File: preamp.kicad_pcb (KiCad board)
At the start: 2 copper layers, 70 x 67 mm, 69 parts, among them J1 AC, J2 JST_XH_3, J3 JST_XH_3, J4 JST_XH_3, J6 JST_XH_3, SW1 SW_SPST, SW2 SW_SPST, U1 L78L09_SOT89, U2 L78L05_SOT89, U3 NJM2753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

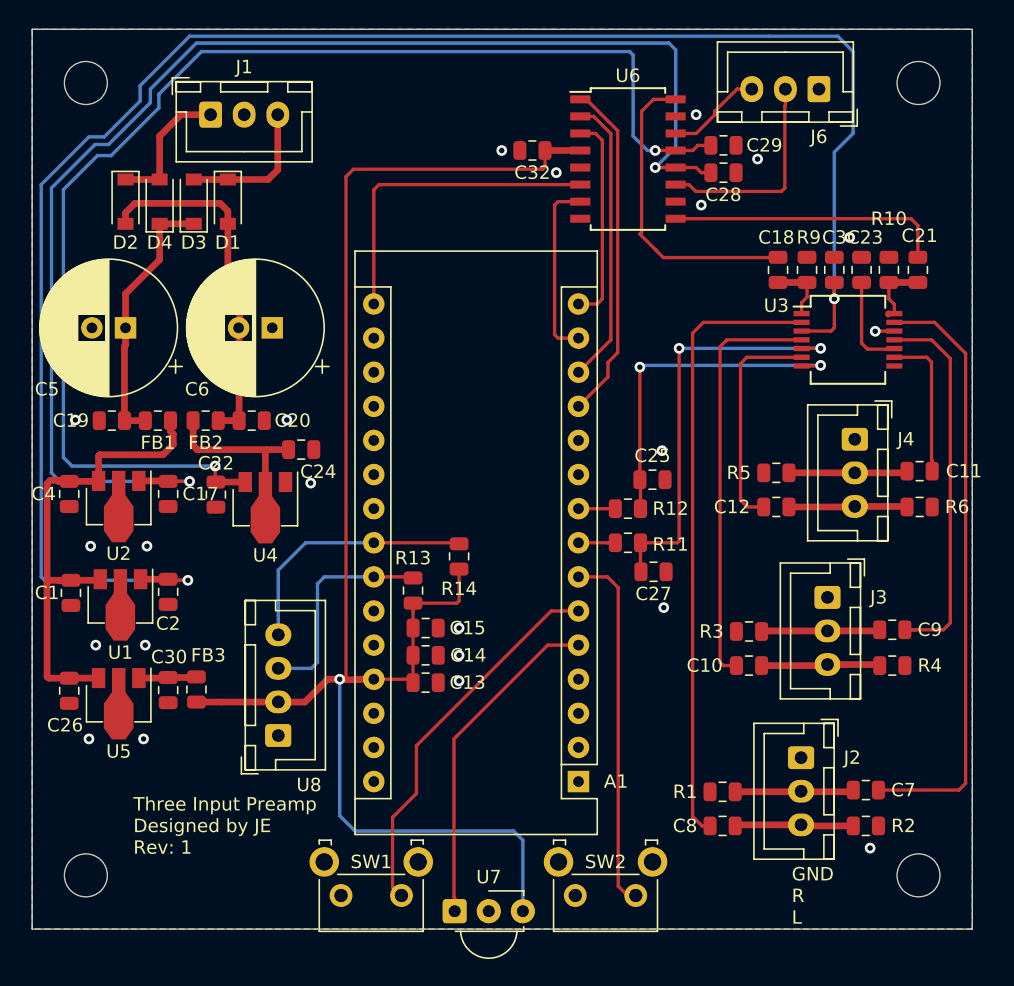
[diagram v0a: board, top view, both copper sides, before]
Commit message: updated silkscreen
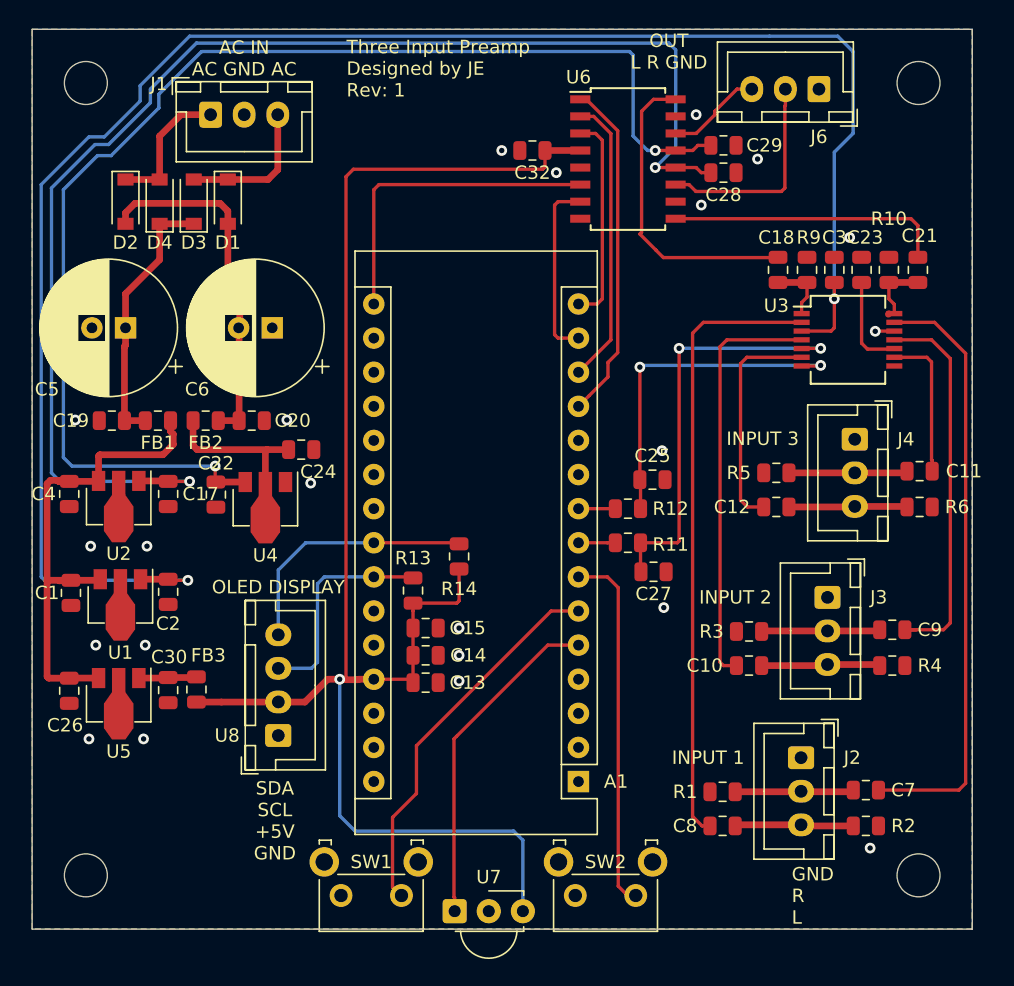
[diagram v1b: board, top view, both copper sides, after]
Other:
- board text added: "AC IN AC GND AC"
- board text added: "INPUT 1"
- board text added: "INPUT 2"
- board text added: "INPUT 3"
- board text added: "OLED DISPLAY"
- board text added: "OUT L R GND"
- board text added: "SDA SCL +5V GND"
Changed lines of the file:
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@@
-(kicad_pcb (version 20171130) (host pcbnew "(5.1.0)-1")
+(kicad_pcb (version 20171130) (host pcbnew 5.0.2-bee76a0~70~ubuntu18.04.1)
   (general
     (thickness 1.6)
-    (drawings 7)
+    (drawings 14)
     (tracks 353)
     (zones 0)
@@
     (zone_45_only no)
     (trace_min 0.2)
+    (segment_width 0.2)
+    (edge_width 0.05)
     (via_size 0.8)
     (via_drill 0.4)
@@
     (uvia_min_size 0.2)
     (uvia_min_drill 0.1)
-    (edge_width 0.05)
-    (segment_width 0.2)
     (pcb_text_width 0.3)
     (pcb_text_size 1.5 1.5)
@@
     (descr "JST XH series connector, B4B-XH-A (http://www.jst-mfg.com/product/pdf/eng/eXH.pdf), generated with kicad-footprint-generator")
     (tags "connector JST XH vertical")
-    (fp_text reference U8 (at -3.683 2.286 180) (layer F.SilkS)
+    (fp_text reference U8 (at 0 -3.81 180) (layer F.SilkS)
       (effects (font (size 1 1) (thickness 0.15)))
     )
@@
     (tags "SOIC 1.27")
     (attr smd)
-    (fp_text reference U6 (at 0 -6.2) (layer F.SilkS)
+    (fp_text reference U6 (at -3.683 -6.096) (layer F.SilkS)
       (effects (font (size 1 1) (thickness 0.15)))
     )
@@
     (descr "JST XH series connector, B3B-XH-A (http://www.jst-mfg.com/product/pdf/eng/eXH.pdf), generated with kicad-footprint-generator")
     (tags "connector JST XH vertical")
-    (fp_text reference J1 (at 2.5 -3.55) (layer F.SilkS)
+    (fp_text reference J1 (at -3.85 -2.286) (layer F.SilkS)
       (effects (font (size 1 1) (thickness 0.15)))
     )
@@
     )
   )
-  (gr_text "Three Input Preamp\nDesigned by JE\nRev: 1" (at 73.533 131.318) (layer F.SilkS)
+  (gr_text "OLED DISPLAY" (at 84.328 113.538) (layer F.SilkS)
+    (effects (font (size 1 1) (thickness 0.15)))
+  )
+  (gr_text "SDA\nSCL\n+5V\nGND" (at 84.074 130.937) (layer F.SilkS)
+    (effects (font (size 1 1) (thickness 0.15)))
+  )
+  (gr_text "INPUT 3" (at 120.396 102.489) (layer F.SilkS)
+    (effects (font (size 1 1) (thickness 0.15)))
+  )
+  (gr_text "INPUT 2" (at 118.364 114.3) (layer F.SilkS)
+    (effects (font (size 1 1) (thickness 0.15)))
+  )
+  (gr_text "INPUT 1" (at 116.332 126.238) (layer F.SilkS)
+    (effects (font (size 1 1) (thickness 0.15)))
+  )
+  (gr_text "OUT\nL R GND" (at 113.411 73.66) (layer F.SilkS)
+    (effects (font (size 1 1) (thickness 0.15)))
+  )
+  (gr_text "AC IN\nAC GND AC" (at 81.788 74.168) (layer F.SilkS)
+    (effects (font (size 1 1) (thickness 0.15)))
+  )
+  (gr_text "Three Input Preamp\nDesigned by JE\nRev: 1" (at 89.408 74.93) (layer F.SilkS)
     (effects (font (size 1 1) (thickness 0.15)) (justify left))
   )

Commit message: tweaks before productioN
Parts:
- C10, C11, C12, C25, C27, C7, C8, C9: value 1u -> 4u7
- C5, C6: value 35V 1500u -> 35V 270u; footprint Capacitor_THT:CP_Radial_D10.0mm_P2.50mm -> Capacitor_SMD:CP_Elec_10x10
- D1, D2, D3, D4: value 1N4001 -> ES1JL
- R11, R12: value 100K -> 47K
- moved C18 2.16 mm to (123.7, 89.9)
- moved C21 2.16 mm to (129.8, 89.9)
- moved R9 2.03 mm to (121.7, 89.9), turned to 270 degrees
- moved R10 2.03 mm to (131.8, 89.9), turned to 270 degrees
- moved C6 0.39 mm to (83.9, 93.9), turned to 270 degrees
- moved C5 0.38 mm to (72.9, 93.9), turned to 90 degrees
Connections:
- R10 pad 1: Net-(C21-Pad1) -> Net-(C21-Pad2)
- R9 pad 1: Net-(C18-Pad2) -> Net-(C18-Pad1)
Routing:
- net Net-(C20-Pad2): track 26.6 -> 29.9 mm
- net Net-(C18-Pad1): track 23.1 -> 26.0 mm
- net /ZCEN: track 25.5 -> 28.1 mm
- net Net-(C21-Pad1): track 4.70 -> 2.49 mm
- net Net-(C18-Pad2): track 4.65 -> 2.49 mm
- net /CS: track 21.6 -> 23.4 mm
- net /CNT1: track 31.4 -> 33.1 mm
- net /SWITCH1: track 28.4 -> 29.0 mm
- net GND: vias 22 -> 25

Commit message: tidied up
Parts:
- moved J1 5.35 mm to (84.3, 76.5), turned to 180 degrees
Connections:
- J1 pad 1: Net-(D2-Pad1) -> Net-(D1-Pad1)
- J1 pad 3: Net-(D1-Pad1) -> Net-(D2-Pad1)
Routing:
- net Net-(D1-Pad1): track 10.7 -> 12.7 mm
- net +9VA: track 134.9 -> 136.1 mm
- net +5VA: track 101.0 -> 102.0 mm
- net -5VA: track 95.0 -> 96.0 mm
- net Net-(D2-Pad1): track 10.2 -> 10.8 mm
